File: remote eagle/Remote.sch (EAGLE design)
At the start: 31 parts, among them IC1 ATmega328p, J1 ISP Touch, Y1 16MHz, Y2 ANTENNA2SMD5, Y3 16MHz

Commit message: Adding screw holes on remote board. Sketching out bottom of enclosure to match screw holes.
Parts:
- added H1, H2: MOUNT-PAD-ROUND3.0, holes:MOUNT-PAD-ROUND3.0
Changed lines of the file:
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@@
 <part name="P+5" library="supply1" deviceset="VCC" device=""/>
 <part name="JP2" library="SparkFun-Connectors" deviceset="M02" device="PTH" value="Serial"/>
+<part name="H1" library="holes" deviceset="MOUNT-PAD-ROUND" device="3.0"/>
+<part name="H2" library="holes" deviceset="MOUNT-PAD-ROUND" device="3.0"/>
 </parts>
 <sheets>
@@
 <instance part="P+5" gate="VCC" x="5.08" y="73.66"/>
 <instance part="JP2" gate="G$1" x="96.52" y="33.02"/>
+<instance part="H1" gate="G$1" x="2.54" y="134.62"/>
+<instance part="H2" gate="G$1" x="2.54" y="127"/>
 </instances>
 <busses>

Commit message: Aligning PCB to bottom enclosure.
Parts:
- removed H1, H2: MOUNT-PAD-ROUND3.0, holes:MOUNT-PAD-ROUND3.0
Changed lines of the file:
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@@
 <part name="P+5" library="supply1" deviceset="VCC" device=""/>
 <part name="JP2" library="SparkFun-Connectors" deviceset="M02" device="PTH" value="Serial"/>
-<part name="H1" library="holes" deviceset="MOUNT-PAD-ROUND" device="3.0"/>
-<part name="H2" library="holes" deviceset="MOUNT-PAD-ROUND" device="3.0"/>
 </parts>
 <sheets>
@@
 <instance part="P+5" gate="VCC" x="5.08" y="73.66"/>
 <instance part="JP2" gate="G$1" x="96.52" y="33.02"/>
-<instance part="H1" gate="G$1" x="2.54" y="134.62"/>
-<instance part="H2" gate="G$1" x="2.54" y="127"/>
 </instances>
 <busses>

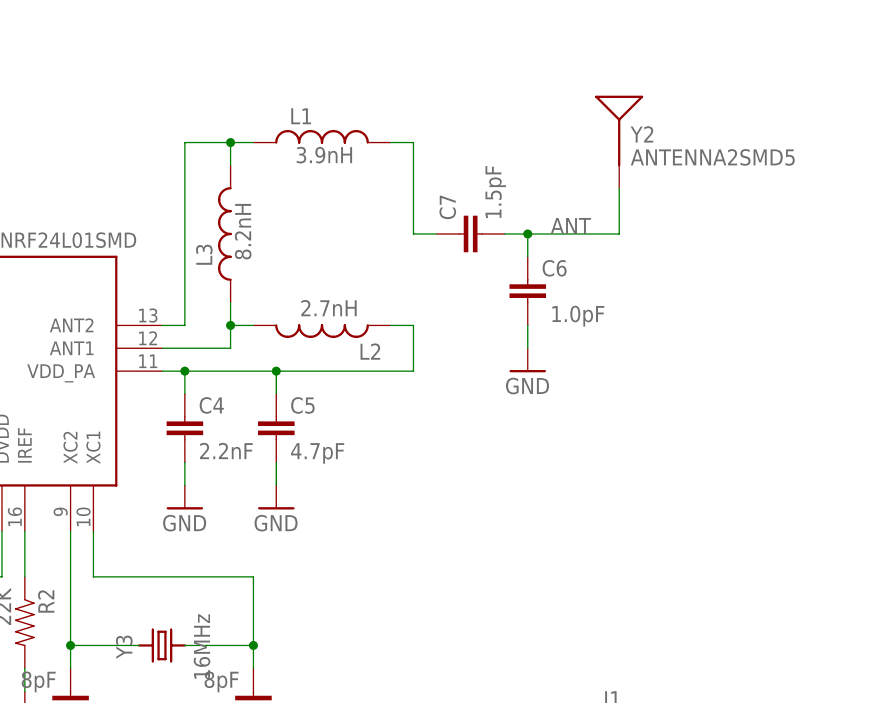
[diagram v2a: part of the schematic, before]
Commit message: Revision 11. Adding balun filter.
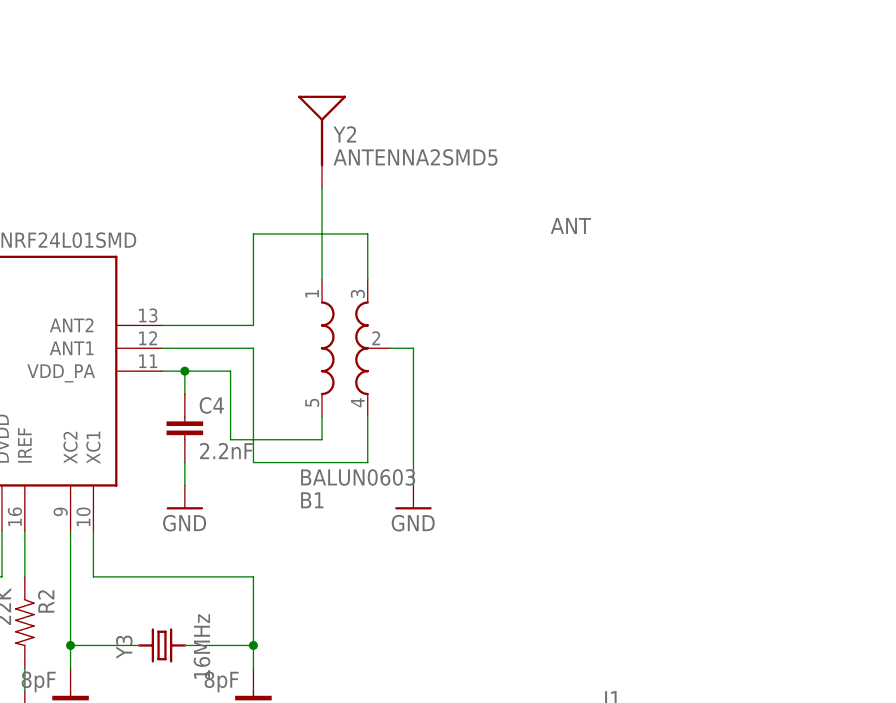
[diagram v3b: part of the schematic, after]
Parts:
- removed C5: 4.7pF, SparkFun:CAP0402-CAP
- removed C6: 1.0pF, SparkFun:CAP0402-CAP
- removed C7: 1.5pF, SparkFun:CAP0402-CAP
- removed L1: 3.9nH, SparkFun:INDUCTOR0402
- removed L2: 2.7nH, SparkFun:INDUCTOR0402
- removed L3: 8.2nH, SparkFun:INDUCTOR0402
- added B1: BALUN0603, remote:BALUN0603
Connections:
- removed net N$6: L1.1, L3.2, NRF24L01QFN.ANT2
- removed net N$8: L2.2, L3.1, NRF24L01QFN.ANT1
- new net N$10: B1.GND@5, C4.1, NRF24L01QFN.VDD_PA
- net ANT: now also B1.IN; no longer C6.2, C7.2
- net GND: now also B1.GND@2; no longer C5.2, C6.1
- net N$7: now also B1.OUT2, NRF24L01QFN.ANT1; no longer C4.1, C5.1, L2.1, NRF24L01QFN.VDD_PA
- net N$9: now also B1.OUT1, NRF24L01QFN.ANT2; no longer C7.1, L1.2
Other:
- moved on the sheet: Y2

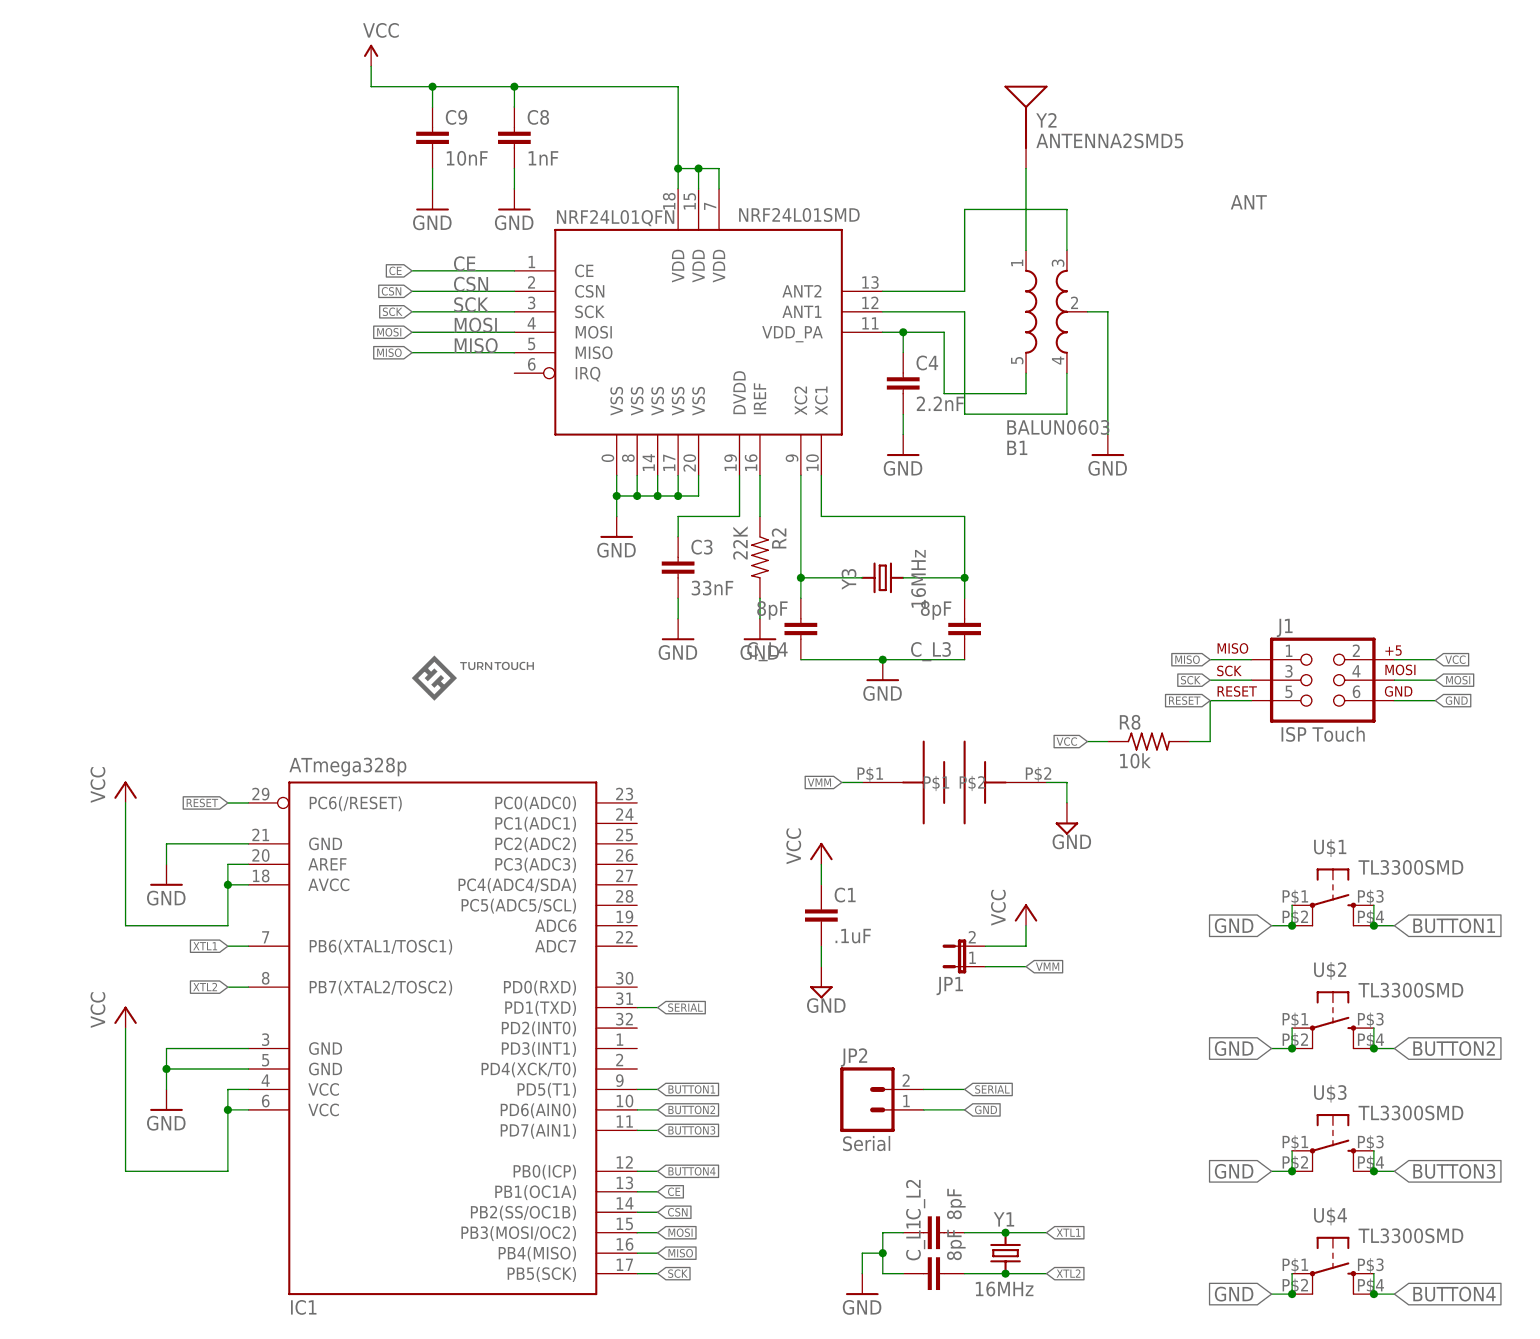
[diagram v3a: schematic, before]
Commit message: Switching from nRF24L01 to RFM22B module on board. All layed out.
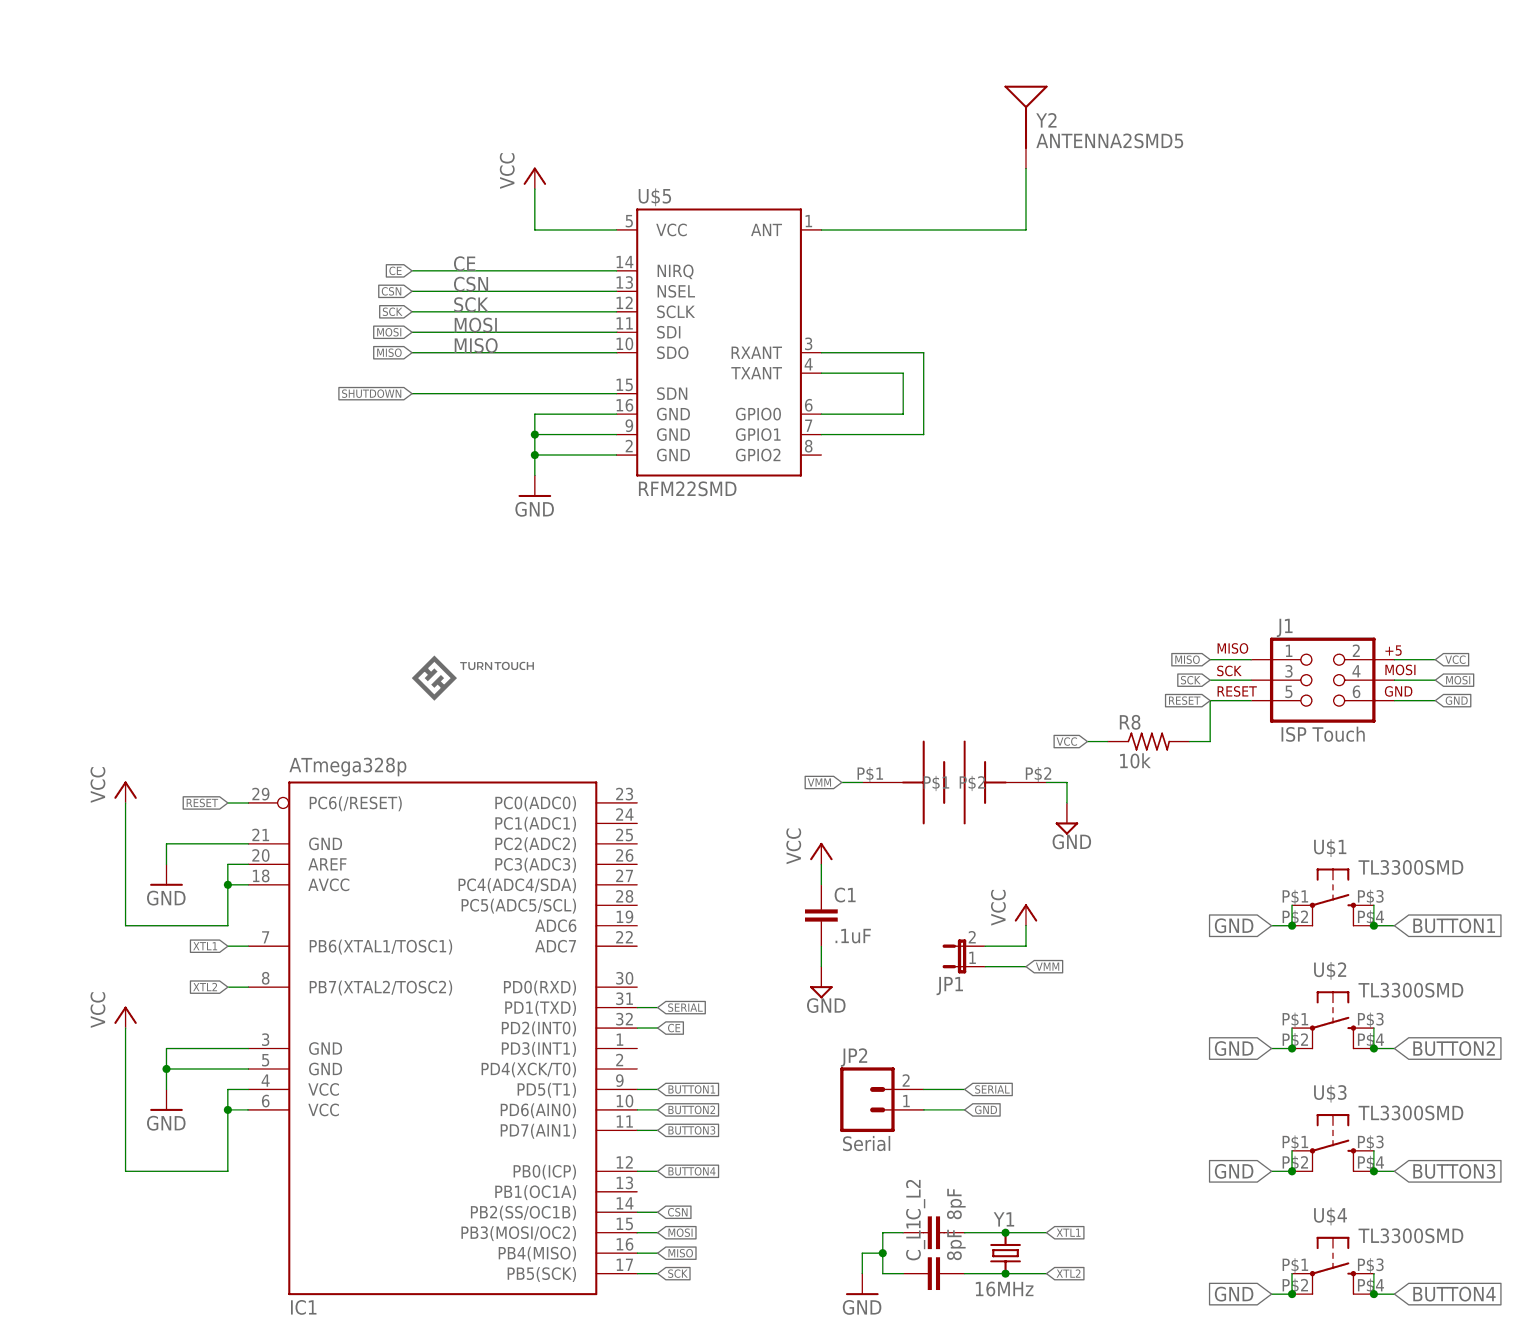
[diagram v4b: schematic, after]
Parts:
- removed B1: BALUN0603, remote:BALUN0603
- removed C3: 33nF, SparkFun:CAP0402-CAP
- removed C4: 2.2nF, SparkFun:CAP0402-CAP
- removed C8: 1nF, SparkFun:CAP0402-CAP
- removed C9: 10nF, SparkFun:CAP0402-CAP
- removed C_L3, C_L4: 8pF, SparkFun-Passives:CAP0402-CAP
- removed NRF24L01QFN: NRF24L01SMD, Testing:NRF24L01SMD
- removed R2: 22K, SparkFun:RESISTOR0402-RES
- removed Y3: 16MHz, remote:CRYSTAL5X3.2
- added U$5: RFM22SMD, remote:RFM22SMD
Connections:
- removed net ANT: B1.IN, Y2.SIGNAL
- removed net N$10: B1.GND@5, C4.1, NRF24L01QFN.VDD_PA
- removed net N$5: C3.1, NRF24L01QFN.DVDD
- removed net N$7: B1.OUT2, NRF24L01QFN.ANT1
- removed net N$9: B1.OUT1, NRF24L01QFN.ANT2
- new net SHUTDOWN: U$5.SDN
- net CE: now also IC1.PD2(INT0), U$5.NIRQ; no longer IC1.PB1(OC1A), NRF24L01QFN.CE
- net CSN: now also U$5.NSEL; no longer NRF24L01QFN.CSN
- net GND: now also U$5.GND@1, U$5.GND@2, U$5.GND@3; no longer B1.GND@2, C3.2, C4.2, C8.2, C9.2, C_L3.1, C_L4.1, NRF24L01QFN.VSS@0, NRF24L01QFN.VSS@14, NRF24L01QFN.VSS@17, NRF24L01QFN.VSS@20, NRF24L01QFN.VSS@8, R2.2
- net MISO: now also U$5.SDO; no longer NRF24L01QFN.MISO
- net MOSI: now also U$5.SDI; no longer NRF24L01QFN.MOSI
- net N$2: now also U$5.ANT, Y2.SIGNAL; no longer C_L4.2, NRF24L01QFN.XC2, Y3.2
- net N$3: now also U$5.GPIO1, U$5.RXANT; no longer C_L3.2, NRF24L01QFN.XC1, Y3.1
- net N$4: now also U$5.GPIO0, U$5.TXANT; no longer NRF24L01QFN.IREF, R2.1
- net SCK: now also U$5.SCLK; no longer NRF24L01QFN.SCK
- net VCC: now also U$5.VCC; no longer C8.1, C9.1, NRF24L01QFN.VDD@15, NRF24L01QFN.VDD@18, NRF24L01QFN.VDD@7
